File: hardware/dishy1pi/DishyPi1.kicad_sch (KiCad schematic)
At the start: 14 parts, among them J1 GPIO, J2 TerminalBlock_2x2.54mm, U1 CAT24C256WI-GT3, U9 CAT24C256WI-GT3

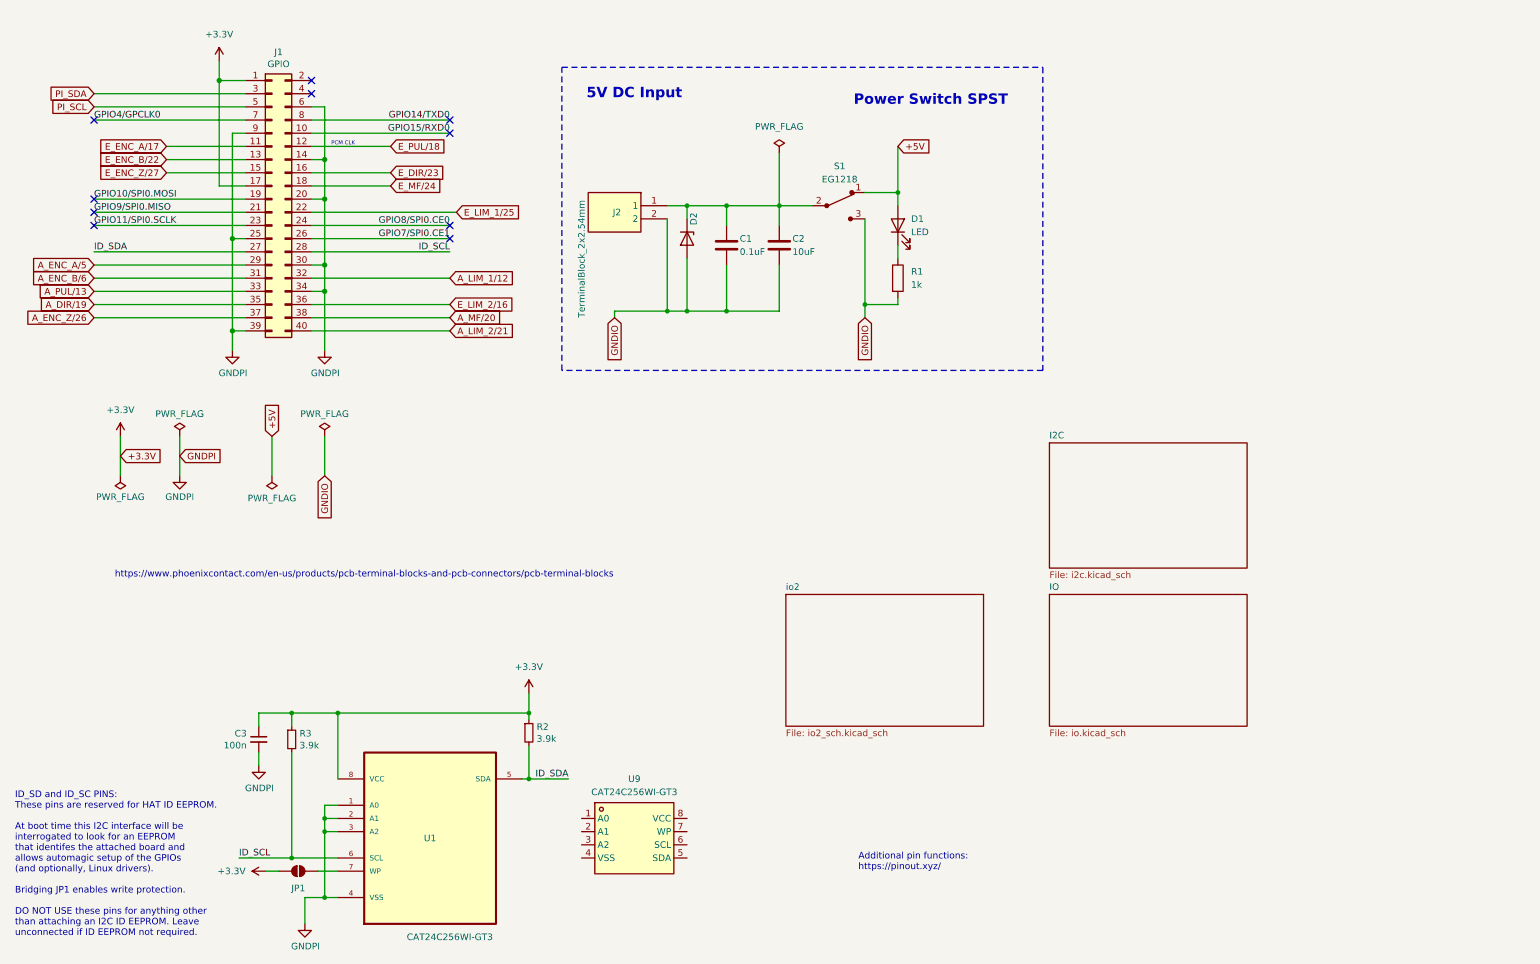
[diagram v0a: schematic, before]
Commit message: Parts place in PCB layout
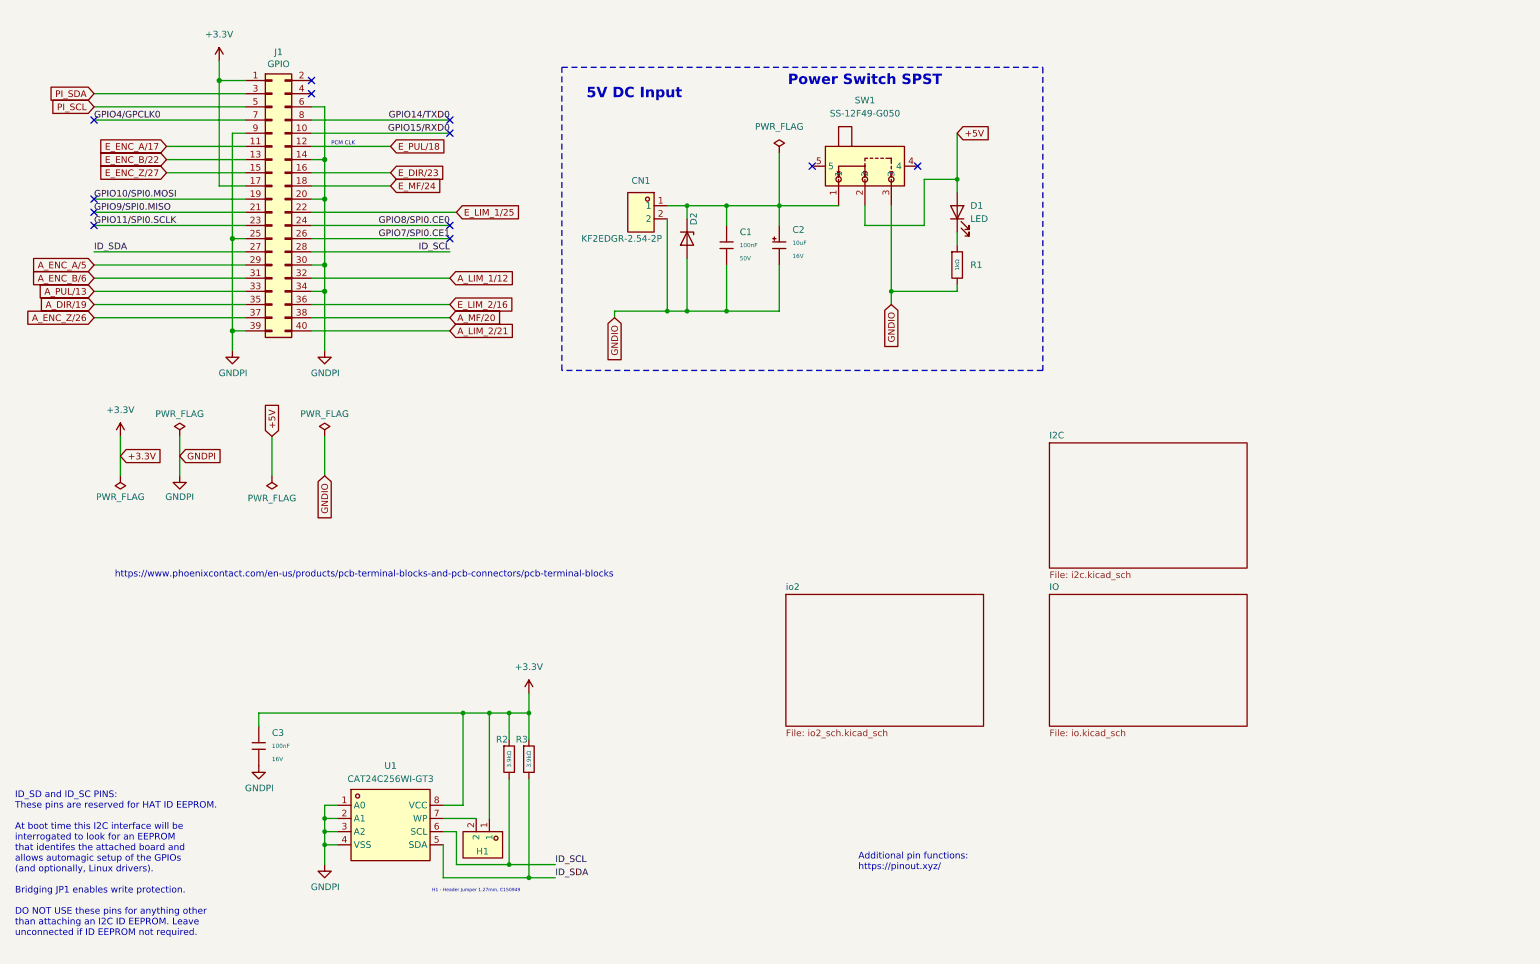
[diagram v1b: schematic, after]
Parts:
- removed C1: 0.1uF, Capacitor_SMD:C_0402_1005Metric, symbol Device:C
- removed C2: 10uF, Capacitor_SMD:C_0402_1005Metric, symbol Device:C
- removed C3: 100n, Capacitor_SMD:C_0402_1005Metric, symbol Device:C_Small
- removed J2: TerminalBlock_2x2.54mm, DishFootprints:TerminalBlock_2x2.54mm, symbol DishSympols:TerminalBlock_2x2.54mm
- removed JP1: JP1, DishFootprints:Header 1x2 Male, symbol Jumper:SolderJumper_2_Open
- removed R1: 1k, Resistor_SMD:R_0402_1005Metric, symbol Device:R
- removed R2, R3: 3.9k, Resistor_SMD:R_0402_1005Metric, symbol Device:R_Small
- removed S1: EG1218, digikey-footprints:Switch_Slide_11.6x4mm_EG1218, symbol dk_Slide-Switches:EG1218
- removed U1: CAT24C256WI-GT3, DishFootprints:CAT24C256_EEPROM, symbol DishSympols:CAT24C256WI-GT3
- added C1: 100nF, PCM_JLCPCB:C_0603, symbol PCM_JLCPCB-Capacitors:0603,100nF
- added C2: 10uF, PCM_JLCPCB:C_CASE-A-3216-18(mm), symbol PCM_JLCPCB-Capacitors:CASE-A-3216-18(mm),10uF
- added C3: 100nF, PCM_JLCPCB:C_0402, symbol PCM_JLCPCB-Capacitors:0402,100nF
- added CN1: KF2EDGR-2.54-2P, MyParts:CONN-TH_P2.54_KF2EDGR-2.54-2P, symbol MyParts:KF2EDGR-2.54-2P
- added H1: 1.27MM/1*2P, MyParts:HDR-TH_2P-P1.27-V-M, symbol MyParts:1.27MM_1*2P
- added R1: 1kΩ, PCM_JLCPCB:R_0805, symbol PCM_JLCPCB-Resistors:0805,1kΩ
- added R2, R3: 3.9kΩ, PCM_JLCPCB:R_0402, symbol PCM_JLCPCB-Resistors:0402,3.9kΩ
- added SW1: SS-12F49-G050, MyParts:SW-TH_SS-12F45-GXXX, symbol MyParts:SS-12F49-G050
- D2: footprint Diode_SMD:D_0402_1005Metric -> Diode_SMD:D_SOD-882
- renumbered U9 to U1
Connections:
- net +3.3V: now also U1.8 (VCC), C3.1, H1.1, R2.1, R3.1
- net +5V: now also SW1.2
- net GNDIO: now also C1.2, C2.2, CN1.2, R1.2, SW1.3
- net GNDPI: now also U1.1 (A0), U1.2 (A1), U1.3 (A2), U1.4 (VSS), C3.2
- net ID_SCL: now also U1.6 (SCL), R2.2
- net ID_SDA: now also U1.5 (SDA), R3.2
- net at D2.1 (K): now also C1.1, C2.1, CN1.1, SW1.1
- net at U1.7 (WP): now also H1.2
- net at D1.1 (K): now also R1.1
- no-connect marks 10 -> 12
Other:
- note added: "H1 - Header Jumper 1.27mm, C150949"
- company: (none) -> JRDish
- moved on the sheet: D1, U1

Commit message: Ground and Power planes placed
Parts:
- D2: value TPESD0402G05V -> PESD5V0L1UL
- J1: value GPIO -> Conn_02x20_Odd_Even
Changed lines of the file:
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@@
 		)
 		(property "Value" "GNDPI"
-			(at 76.3143 84.3344 0)
+			(at 76.2 83.82 0)
 			(effects
 				(font
@@
 					(size 1.27 1.27)
 				)
+				(hide yes)
 			)
 		)
@@
 					(size 1.27 1.27)
 				)
+				(hide yes)
 			)
 		)
@@
 		)
 		(property "Value" "GNDPI"
-			(at 58.5343 84.3344 0)
+			(at 58.42 83.82 0)
 			(effects
 				(font
@@
 					(size 1.27 1.27)
 				)
+				(hide yes)
 			)
 		)
@@
 					(size 1.27 1.27)
 				)
+				(hide yes)
 			)
 		)
@@
 		(dnp no)
 		(property "Reference" "J1"
-			(at 67.31 22.4598 0)
-			(effects
-				(font
-					(size 1.27 1.27)
-				)
-			)
-		)
-		(property "Value" "GPIO"
-			(at 67.31 24.765 0)
+			(at 67.31 25.4 0)
+			(effects
+				(font
+					(size 1.27 1.27)
+				)
+			)
+		)
+		(property "Value" "Conn_02x20_Odd_Even"
+			(at 67.31 78.74 0)
 			(effects
 				(font
@@
 		)
 		(property "Footprint" "Connector_PinSocket_2.54mm:PinSocket_2x20_P2.54mm_Vertical"
-			(at -57.15 74.93 0)
+			(at 66.04 50.8 0)
 			(effects
 				(font
@@
 		)
 		(property "Datasheet" "~"
-			(at -57.15 74.93 0)
+			(at 66.04 50.8 0)
 			(effects
 				(font
@@
 		)
 		(property "Value" "PWR_FLAG"
-			(at 66.04 108.458 0)
+			(at 66.04 107.95 0)
 			(effects
 				(font
@@
 		(dnp no)
 		(property "Reference" "R2"
-			(at 109.22 154.94 0)
+			(at 113.538 158.75 0)
 			(effects
 				(font
@@
 		(dnp no)
 		(property "Reference" "H1"
-			(at 105.41 176.53 90)
-			(effects
-				(font
-					(size 1.27 1.27)
-				)
-				(justify left)
+			(at 113.03 175.26 0)
+			(effects
+				(font
+					(size 1.27 1.27)
+				)
 			)
 		)
 		(property "Value" "1.27MM/1*2P"
-			(at 104.14 176.53 90)
-			(effects
-				(font
-					(size 1.27 1.27)
-				)
-				(justify left)
-				(hide yes)
+			(at 100.33 175.26 0)
+			(effects
+				(font
+					(size 1.27 1.27)
+				)
 			)
 		)
@@
 		)
 		(property "Value" "GNDPI"
-			(at 76.3143 183.3944 0)
+			(at 76.2 182.88 0)
 			(effects
 				(font
@@
 					(size 1.27 1.27)
 				)
+				(hide yes)
 			)
 		)
@@
 					(size 1.27 1.27)
 				)
+				(hide yes)
 			)
 		)
@@
 		)
 		(property "Value" "PWR_FLAG"
-			(at 76.2 92.202 0)
+			(at 76.2 92.71 0)
 			(effects
 				(font
@@
 		(dnp no)
 		(property "Reference" "CN1"
-			(at 137.16 47.244 0)
+			(at 137.16 46.99 0)
 			(effects
 				(font
@@
 		)
 		(property "Value" "KF2EDGR-2.54-2P"
-			(at 141.224 58.42 0)
-			(effects
-				(font
-					(size 1.27 1.27)
-				)
-				(justify left)
+			(at 137.16 59.69 0)
+			(effects
+				(font
+					(size 1.27 1.27)
+				)
 			)
 		)
@@
 		(dnp no)
 		(property "Reference" "R3"
-			(at 113.03 154.94 0)
+			(at 117.348 158.75 0)
 			(effects
 				(font
@@
 		)
 		(property "Value" "GNDPI"
-			(at 63.6143 164.3444 0)
+			(at 63.5 163.83 0)
 			(effects
 				(font
@@
 					(size 1.27 1.27)
 				)
+				(hide yes)
 			)
 		)
@@
 					(size 1.27 1.27)
 				)
+				(hide yes)
 			)
 		)
@@
 		(dnp no)
 		(property "Reference" "D2"
-			(at 147.32 54.61 0)
-			(effects
-				(font
-					(size 1.27 1.27)
-				)
-			)
-		)
-		(property "Value" "TPESD0402G05V"
-			(at 146.05 73.66 0)
-			(effects
-				(font
-					(size 1.27 1.27)
-				)
-				(hide yes)
+			(at 148.59 58.42 0)
+			(effects
+				(font
+					(size 1.27 1.27)
+				)
+			)
+		)
+		(property "Value" "PESD5V0L1UL"
+			(at 143.51 58.42 0)
+			(effects
+				(font
+					(size 1.27 1.27)
+				)
 			)
 		)
@@
 		(dnp no)
 		(property "Reference" "D1"
-			(at 200.66 52.07 90)
-			(effects
-				(font
-					(size 1.27 1.27)
-				)
-				(justify right)
+			(at 195.58 53.34 0)
+			(effects
+				(font
+					(size 1.27 1.27)
+				)
 			)
 		)
 		(property "Value" "LED"
-			(at 200.66 54.61 90)
-			(effects
-				(font
-					(size 1.27 1.27)
-				)
-				(justify right)
+			(at 200.66 53.34 0)
+			(effects
+				(font
+					(size 1.27 1.27)
+				)
 			)
 		)
@@
 		)
 		(property "Value" "PWR_FLAG"
-			(at 36.83 108.204 0)
+			(at 36.83 107.95 0)
 			(effects
 				(font
@@
 		)
 		(property "Value" "GNDPI"
-			(at 48.26 108.204 0)
+			(at 48.26 107.95 0)
 			(effects
 				(font
@@
 		)
 		(property "Value" "PWR_FLAG"
-			(at 48.26 92.202 0)
-			(effects
-				(font
+			(at 48.26 92.71 0)
+			(effects
+				(font

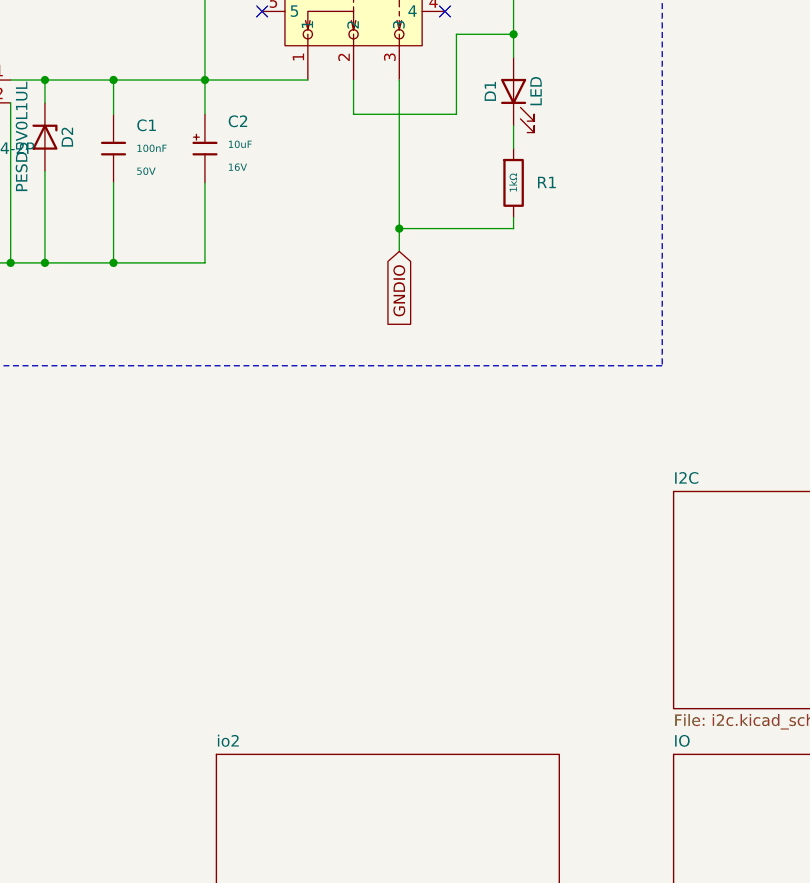
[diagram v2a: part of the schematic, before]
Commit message: Modifications based on first board assembly
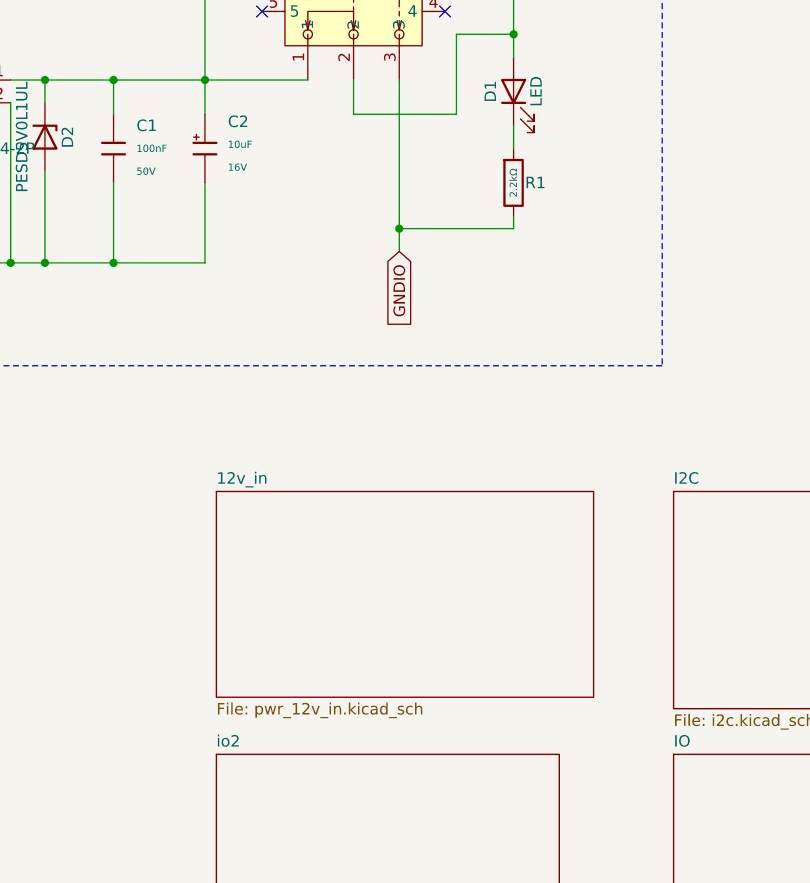
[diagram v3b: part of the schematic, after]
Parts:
- removed R1: 1kΩ, PCM_JLCPCB:R_0805, symbol PCM_JLCPCB-Resistors:0805,1kΩ
- added R1: 2.2kΩ, PCM_JLCPCB:R_0402, symbol PCM_JLCPCB-Resistors:0402,2.2kΩ
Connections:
- net GNDIO: now also R1.2
- net at D1.1 (K): now also R1.1
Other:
- added sheet 12v_in (pwr_12v_in.kicad_sch)

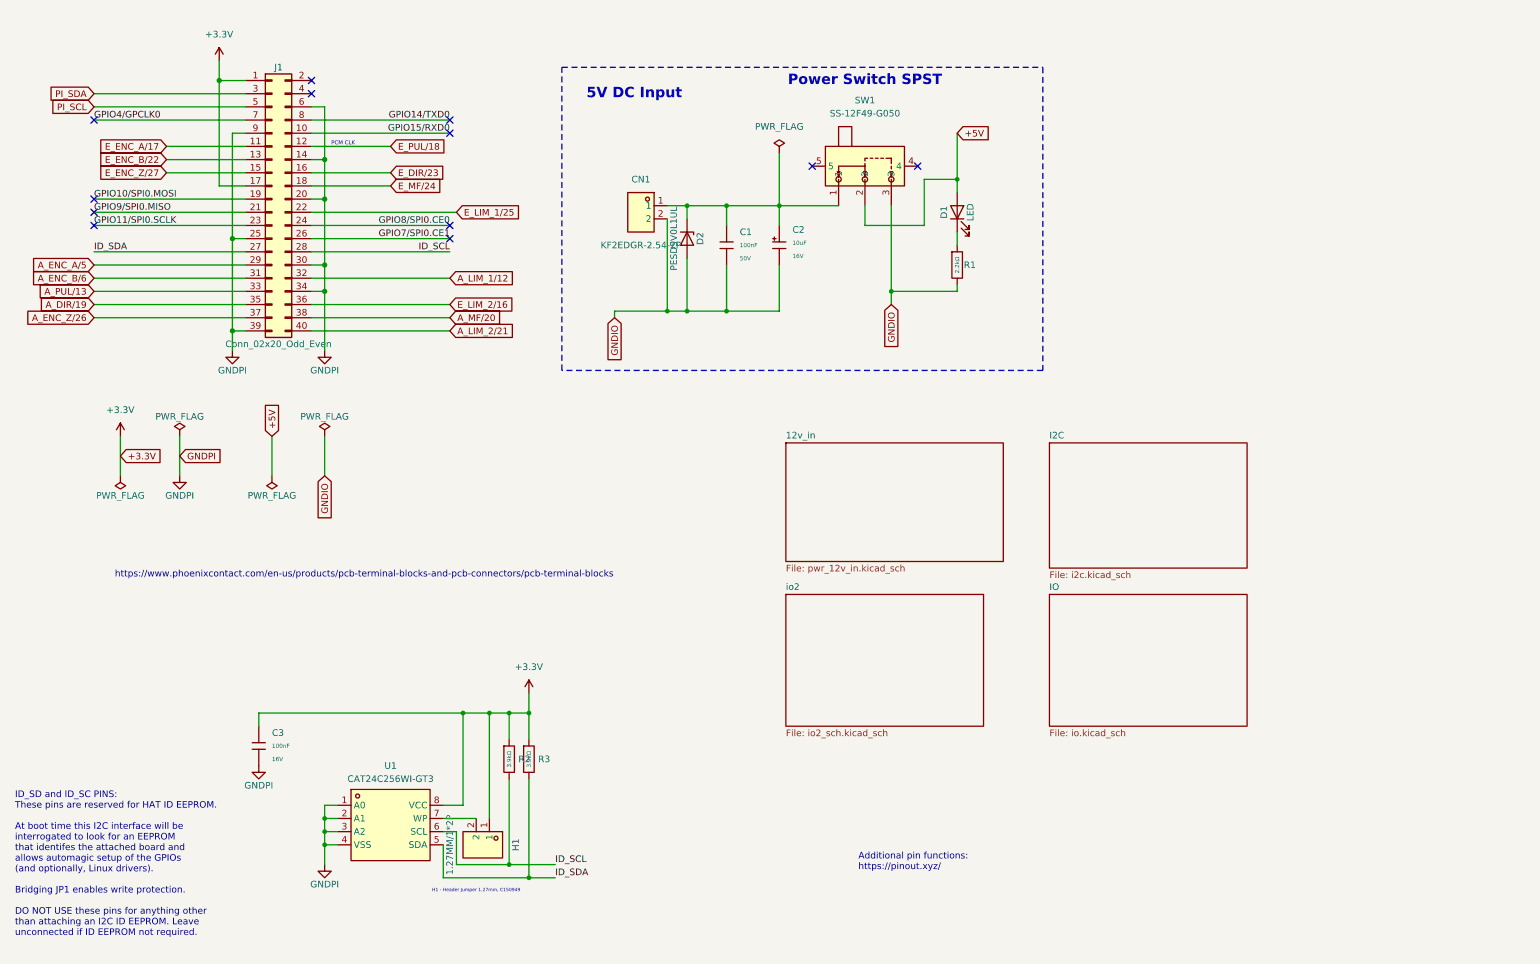
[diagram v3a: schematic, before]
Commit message: Added power circuit to dishy schematic
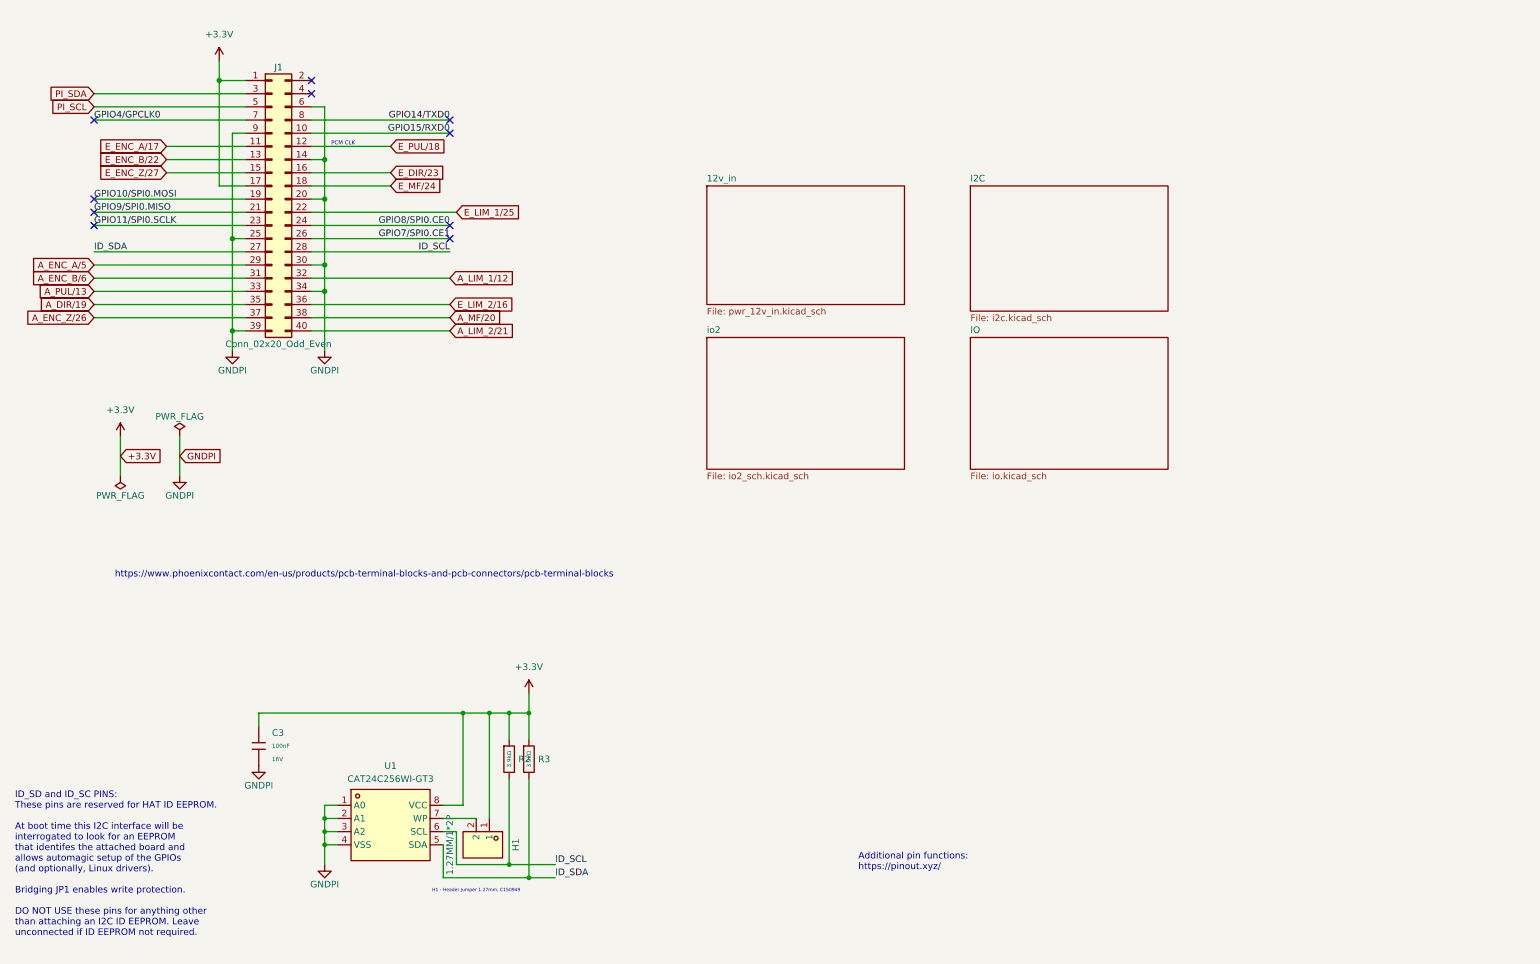
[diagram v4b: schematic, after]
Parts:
- removed C1: 100nF, PCM_JLCPCB:C_0603, symbol PCM_JLCPCB-Capacitors:0603,100nF
- removed C2: 10uF, PCM_JLCPCB:C_CASE-A-3216-18(mm), symbol PCM_JLCPCB-Capacitors:CASE-A-3216-18(mm),10uF
- removed CN1: KF2EDGR-2.54-2P, MyParts:CONN-TH_P2.54_KF2EDGR-2.54-2P, symbol MyParts:KF2EDGR-2.54-2P
- removed D1: LED, LED_SMD:LED_1206_3216Metric, symbol Device:LED
- removed D2: PESD5V0L1UL, Diode_SMD:D_SOD-882, symbol Diode:PESD5V0L1UL
- removed R1: 2.2kΩ, PCM_JLCPCB:R_0402, symbol PCM_JLCPCB-Resistors:0402,2.2kΩ
- removed SW1: SS-12F49-G050, MyParts:SW-TH_SS-12F45-GXXX, symbol MyParts:SS-12F49-G050
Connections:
- no-connect marks 12 -> 10
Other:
- note removed: "5V DC Input"
- note removed: "Power Switch SPST"
